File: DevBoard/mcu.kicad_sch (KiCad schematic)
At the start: 46 parts, among them J301 SWD, J302 UART debug, J303 Spare GPIO, SW301 RESET, U301 STM32WB1MMC

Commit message: Dev board: open-item pass, J104 diode, antenna keep-out, bring-up checklist
- D104 SS34 in series with the J104 bench input (reversed lead, back-feed).
- ANT_KEEPOUT rule area (no tracks/vias/pours, all copper layers) around
  the STM32WB1MMC antenna end, created by place_parts.py.
- D401 drawn unidirectional; header part numbers (PZ254V-11 family);
  shunt, J301 keying, B-constant, insulated-NTC, sheet-text and R201 notes.
- docs/devboard/bringup-config-checklist.md: every configuration item from
  both reviews in bring-up order, with review 2's precharge correction;
  review 1's 0 mV precharge line marked superseded.

Co-Authored-By: Claude Opus 5.5 <noreply@anthropic.com>
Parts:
- J301: Notes Keyed (pin 7 removed) so standard Cortex debug cables only 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 -> Keyed by its shroud (-K): Cortex 10-pin cables seat one way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
- J302: LCSC (none) -> C2937625; MPN (none) -> PZ254V-11-03P
- J303: LCSC (none) -> C492406; MPN (none) -> PZ254V-11-07P
- TH301: Notes TH1 port 1 stage -> TH1 port 1 stage. Murata NCP18XH103F03RB: B25/50 = 3380 K, 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
- TH302: Notes TH2 port 2 stage -> TH2 port 2 stage. Murata NCP18XH103F03RB: B25/50 = 3380 K, 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
- TH303: Notes TH3 connectors -> TH3 connectors. Murata NCP18XH103F03RB: B25/50 = 3380 K, B2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
- TH304: Notes TH4 heatsink pad -> TH4 heatsink pad. Murata NCP18XH103F03RB: B25/50 = 3380 K, 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
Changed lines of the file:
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@@
 			)
 		)
-		(property "Notes" "TH2 port 2 stage"
+		(property "Notes" "TH2 port 2 stage. Murata NCP18XH103F03RB: B25/50 = 3380 K, B25/85 = 3435 K (the \"B3435\" in the value); use Murata's R-T table in firmware"
 			(at 0 0 0)
 			(hide yes)
@@
 			)
 		)
-		(property "Notes" "TH3 connectors"
+		(property "Notes" "TH3 connectors. Murata NCP18XH103F03RB: B25/50 = 3380 K, B25/85 = 3435 K (the \"B3435\" in the value); use Murata's R-T table in firmware"
 			(at 0 0 0)
 			(hide yes)
@@
 			)
 		)
-		(property "Notes" "TH4 heatsink pad"
+		(property "Notes" "TH4 heatsink pad. Murata NCP18XH103F03RB: B25/50 = 3380 K, B25/85 = 3435 K (the \"B3435\" in the value); use Murata's R-T table in firmware"
 			(at 0 0 0)
 			(hide yes)
@@
 			)
 		)
-		(property "Notes" "Keyed (pin 7 removed) so standard Cortex debug cables only fit one way (review m15)"
+		(property "Notes" "Keyed by its shroud (-K): Cortex 10-pin cables seat one way only (review m15; all 10 pins fitted, pin 7 is NOT removed). Hand-fit, not in the JLC BOM"
 			(at -148.59 40.64 0)
 			(hide yes)
@@
 			)
 		)
-		(property "Notes" "TH1 port 1 stage"
+		(property "Notes" "TH1 port 1 stage. Murata NCP18XH103F03RB: B25/50 = 3380 K, B25/85 = 3435 K (the \"B3435\" in the value); use Murata's R-T table in firmware"
 			(at 0 0 0)
 			(hide yes)
@@
 			)
 		)
+		(property "LCSC" "C2937625"
+			(at 304.8 137.16 0)
+			(hide yes)
+			(show_name no)
+			(do_not_autoplace no)
+			(effects
+				(font
+					(size 1.27 1.27)
+				)
+			)
+		)
+		(property "MPN" "PZ254V-11-03P"
+			(at 304.8 137.16 0)
+			(hide yes)
+			(show_name no)
+			(do_not_autoplace no)
+			(effects
+				(font
+					(size 1.27 1.27)
+				)
+			)
+		)
 		(pin "1"
 		)
@@
 			(at 304.8 165.1 0)
 			(hide yes)
+			(show_name no)
+			(do_not_autoplace no)
+			(effects
+				(font
+					(size 1.27 1.27)
+				)
+			)
+		)
+		(property "LCSC" "C492406"
+			(at 304.8 165.1 0)
+			(hide yes)
+			(show_name no)
+			(do_not_autoplace no)
+			(effects
+				(font
+					(size 1.27 1.27)
+				)
+			)
+		)
+		(property "MPN" "PZ254V-11-07P"
+			(at 304.8 165.1 0)
+			(hide yes)

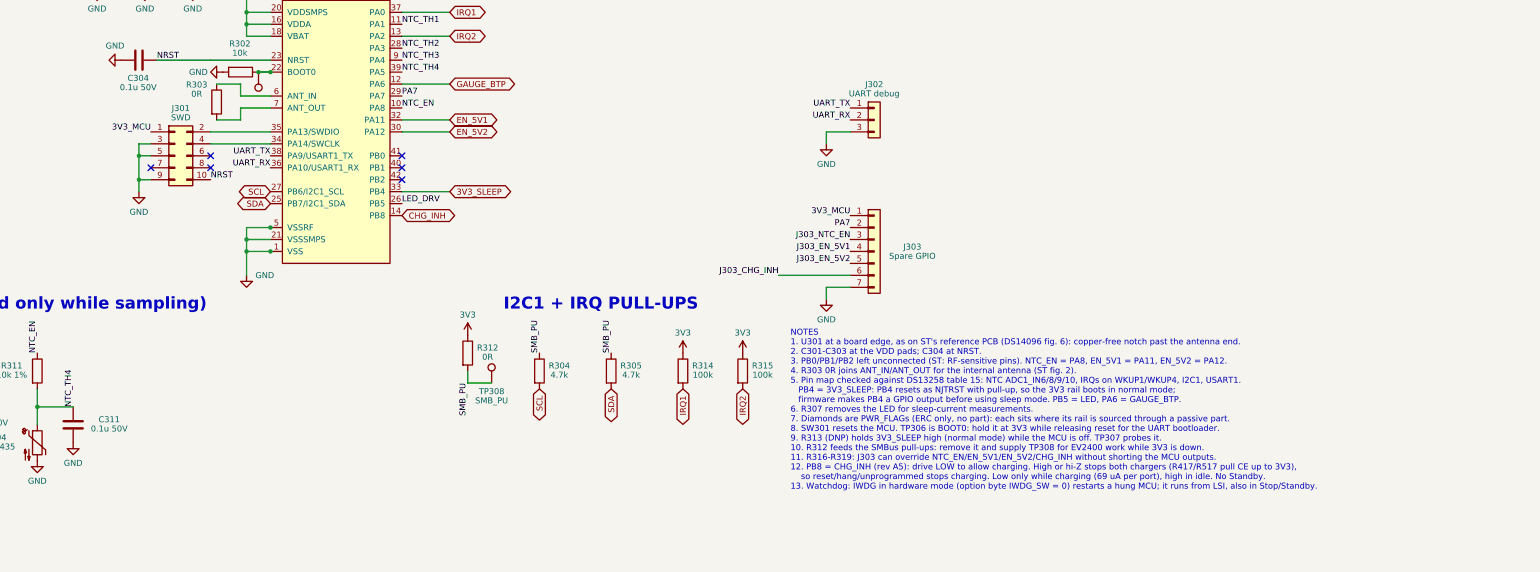
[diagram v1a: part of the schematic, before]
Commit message: Dev board: TH305 at the protection FETs; drop the gauge-BAT INA190 idea
- TH305 (10k NTC) between Q101/Q102 on PA7 / ADC1_IN2, same 10k 1 % /
  0.1 uF divider from NTC_EN (R320, C312). PA7 net renamed NTC_TH5, still
  on J303 pin 2. Placed beside C111; R320/C312 under J303.
- Optional third INA190 on the gauge BAT feed dropped: measure the gauge
  supply as the drop across R105 (100 R, 50-340 uA = 5-34 mV).

Co-Authored-By: Claude Opus 5.5 <noreply@anthropic.com>
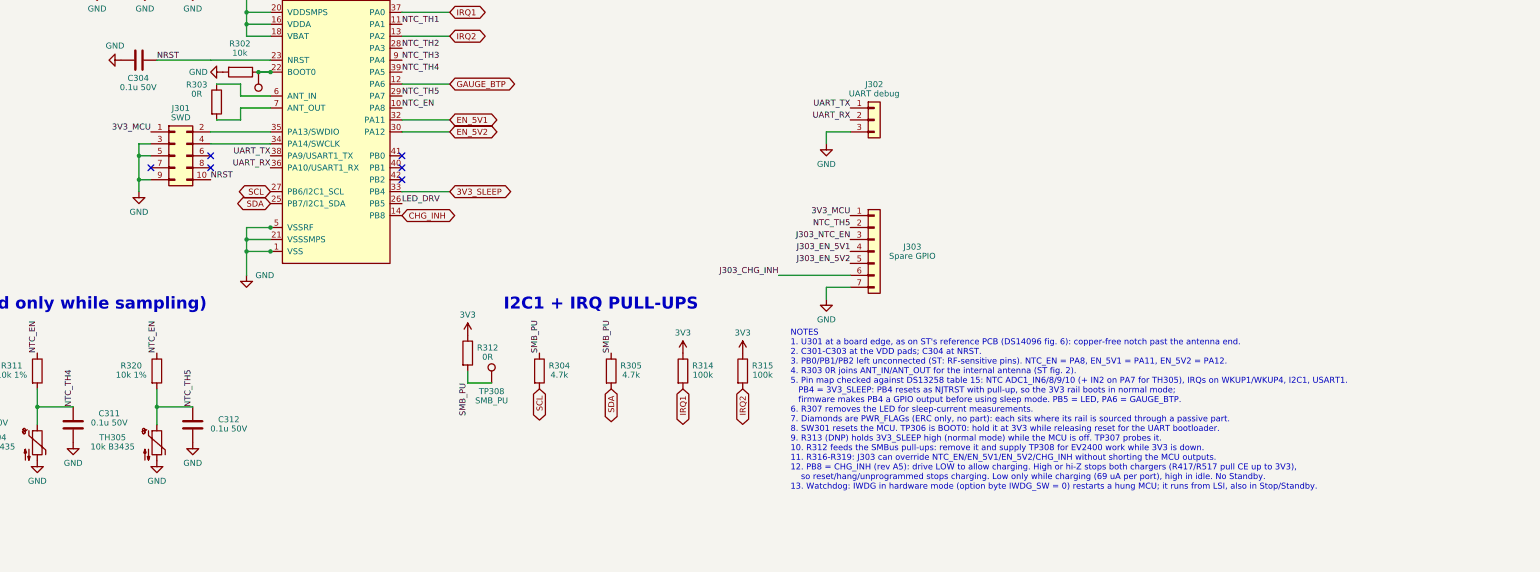
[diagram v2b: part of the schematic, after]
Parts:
- added C312: 0.1u 50V, Capacitor_SMD:C_0603_1608Metric, symbol Device:C
- added R320: 10k 1%, Resistor_SMD:R_0805_2012Metric, symbol Device:R
- added TH305: 10k B3435, Resistor_SMD:R_0603_1608Metric, symbol Device:Thermistor_NTC
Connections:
- net GND: now also C312.2, TH305.2
- net NTC_EN: now also R320.1
- net PA7 renamed NTC_TH5
- net NTC_TH5: now also C312.1, R320.2, TH305.1
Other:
- note added: "NOTES 1. U301 at a board edge, as on ST's reference PCB (DS14096 fig. 6): copper-free notch past the antenna end. 2. C301-C303 at the VDD pads; C304 at NRST. 3. PB0/PB1/PB2 left unconnected (ST: RF-sensitive pins). NTC_EN = PA8, EN_5V1 = PA11, EN_5V2 = PA12. 4. R303 0R joins ANT_IN/ANT_OUT for the internal antenna (ST fig. 2). 5. Pin map checked against DS13258 table 15: NTC ADC1_IN6/8/9/10 (+ IN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"
- note removed: "NOTES 1. U301 at a board edge, as on ST's reference PCB (DS14096 fig. 6): copper-free notch past the antenna end. 2. C301-C303 at the VDD pads; C304 at NRST. 3. PB0/PB1/PB2 left unconnected (ST: RF-sensitive pins). NTC_EN = PA8, EN_5V1 = PA11, EN_5V2 = PA12. 4. R303 0R joins ANT_IN/ANT_OUT for the internal antenna (ST fig. 2). 5. Pin map checked against DS13258 table 15: NTC ADC1_IN6/8/9/10, IRQs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"

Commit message: Dev board: holder tab hole, Samtec J301 land pattern, 3D models, measured USB-C STEP
- Cell holder footprint: add the dia 2.25 hole for the + terminal locating
  tab (from the rendered MYOUNG drawing; the holder could not seat flat).
- J301 on Samtec's recommended FTSH-1xx-DV land pattern with the -K shroud
  courtyard; J301 and the MCU title moved to fit.
- 3D models on 292 of 362 footprints: custom footprints borrow same-body
  KiCad models (pin 1 checked in renders); SMA and TS-1187A re-pointed to
  shipped models by place_parts.py.
- USB-C (J401/J501): STEP model measured from ShouHan's vector drawing
  (tools/drawing_extract, tools/make_3d_usbc.py) and verified by hidden-line
  overlays on all three views (3dmodels/verification).
- Placer: test-point labels sorted by reference; hidden only when no spot.
- docs/devboard/power-budget.md; renders in DevBoard/renders.

Co-Authored-By: Claude Opus 5.5 <noreply@anthropic.com>
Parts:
- J301: footprint Connector_PinHeader_1.27mm:PinHeader_2x05_P1.27mm_Vertical_SMD -> MonolithDev:Samtec_FTSH-105-01-xx-DV-K_2x05_P1.27mm
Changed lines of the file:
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@@
 			)
 		)
-		(property "Footprint" "Connector_PinHeader_1.27mm:PinHeader_2x05_P1.27mm_Vertical_SMD"
+		(property "Footprint" "MonolithDev:Samtec_FTSH-105-01-xx-DV-K_2x05_P1.27mm"
 			(at 156.21 144.78 0)
 			(hide yes)

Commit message: Dev board: cost-down pass (about $113 -> $80 per board at 5 boards)
Swaps from docs/devboard/cost-down-2026-10-14.md, datasheet-checked:
- L401/L501 XAL7030 -> SMMS1040-2R2M (Isat 18 A, Irms 12 A, 9 mOhm)
- L402/L502 SRP5030T -> APS0530M3R3H (new footprint L_Coilank_APS0530)
- L201 SRN4018TA -> FNR4030S100MT
- U203 TPS70950 -> HT7550-1, C204/C205 10 uF per Holtek's basic circuit
- C431/C434/C435 47 uF 1210 -> 22 uF 1206 (bank ~114 uF effective)
- JLC basic/preferred equivalents: D103, D401, R410/R412, C105/C206,
  C406, Q103 -> AO3400A
- D301 (out of stock) -> red KT-0603R
- R431/R531 -> bridged solder jumper
- 34 test loops -> bare pads; pin headers hand-soldered
- U301 bought from ST and consigned to JLC

ERC unchanged (0 errors, 8 expected GPIO-to-GND warnings).

Co-Authored-By: Claude Opus 5.5 <noreply@anthropic.com>
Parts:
- D301: value Green status -> Red status; LCSC C72043 -> C2286; MPN 19-217/GHC-YR1S2/3T -> KT-0603R (Hubei KENTO); Notes (none) -> Red 0603 (Vf 1.8-2.4 V), JLC basic: about 4 mA through R306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
- J302: LCSC C2937625 -> (none); Sourcing (none) -> Hand-solder, not JLC assembled (through-hole; LCSC C2937625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
- J303: LCSC C492406 -> (none); Sourcing (none) -> Hand-solder, not JLC assembled (through-hole; LCSC C492406 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
- R306: Notes InGaN green (Vf ~3 V): 330R gives ~1 mA from 3.3 V (1k gave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 -> 330R with the red KT-0603R (Vf ~2 V): about 4 mA from 3.3 V
- TP301, TP302, TP303, TP304, TP305, TP308: footprint MonolithDev:TestPoint_Harwin_S2761_0603 -> TestPoint:TestPoint_Pad_D1.5mm; LCSC C55121754 -> (none); MPN RH-S2761-46R (ronghe; Harwin S2761-46R equivalent) -> (none); now left out of the parts list
- U301: Notes LGA-77, JLC-placed only: check JLC stock at order time (LCS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 -> LGA-77: have JLC place it from consigned stock (JLC had 0 o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; Sourcing (none) -> Buy from ST eStore ($10.65 at 1, $9.87 at 10 on 2026-10-14)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
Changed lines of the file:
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@@
 			)
 		)
-		(property "Value" "Green status"
+		(property "Value" "Red status"
 			(at 71.43 239.77 0)
 			(show_name no)
@@
 			)
 		)
+		(property "Notes" "Red 0603 (Vf 1.8-2.4 V), JLC basic: about 4 mA through R306. The green Everlight 19-217 (C72043) went out of stock at JLC (cost-down 2026-10-14)"
+			(at 71.12 243.84 0)
+			(hide yes)
+			(show_name no)
+			(do_not_autoplace no)
+			(effects
+				(font
+					(size 1.27 1.27)
+				)
+			)
+		)
 		(property "Description" "Light emitting diode"
 			(at 71.12 243.84 0)
@@
 			)
 		)
-		(property "LCSC" "C72043"
+		(property "LCSC" "C2286"
 			(at 71.12 243.84 0)
 			(hide yes)
@@
 			)
 		)
-		(property "MPN" "19-217/GHC-YR1S2/3T"
+		(property "MPN" "KT-0603R (Hubei KENTO)"
 			(at 71.12 243.84 0)
 			(hide yes)
@@
 		(body_style 1)
 		(exclude_from_sim no)
-		(in_bom yes)
+		(in_bom no)
 		(on_board yes)
 		(in_pos_files yes)
@@
 			)
 		)
-		(property "Footprint" "MonolithDev:TestPoint_Harwin_S2761_0603"
+		(property "Footprint" "TestPoint:TestPoint_Pad_D1.5mm"
 			(at 223.52 193.04 0)
 			(hide yes)
@@
 			)
 		)
-		(property "LCSC" "C55121754"
-			(at 223.52 193.04 0)
-			(hide yes)
-			(show_name no)
-			(do_not_autoplace no)
-			(effects
-				(font
-					(size 1.27 1.27)
-				)
-			)
-		)
-		(property "MPN" "RH-S2761-46R (ronghe; Harwin S2761-46R equivalent)"
-			(at 223.52 193.04 0)
-			(hide yes)
-			(show_name no)
-			(do_not_autoplace no)
-			(effects
-				(font
-					(size 1.27 1.27)
-				)
-			)
-		)
 		(pin "1"
 		)
@@
 		(body_style 1)
 		(exclude_from_sim no)
-		(in_bom yes)
+		(in_bom no)
 		(on_board yes)
 		(in_pos_files yes)
@@
 			)
 		)
-		(property "Footprint" "MonolithDev:TestPoint_Harwin_S2761_0603"
+		(property "Footprint" "TestPoint:TestPoint_Pad_D1.5mm"
 			(at 236.22 264.16 0)
 			(hide yes)
@@
 			)
 		)
-		(property "LCSC" "C55121754"
-			(at 231.14 264.16 0)
-			(hide yes)
-			(show_name no)
-			(do_not_autoplace no)
-			(effects
-				(font
-					(size 1.27 1.27)
-				)
-			)
-		)
-		(property "MPN" "RH-S2761-46R (ronghe; Harwin S2761-46R equivalent)"
-			(at 231.14 264.16 0)
-			(hide yes)
-			(show_name no)
-			(do_not_autoplace no)
-			(effects
-				(font
-					(size 1.27 1.27)
-				)
-			)
-		)
 		(pin "1"
 		)
@@
 			)
 		)
+		(property "Sourcing" "Buy from ST eStore ($10.65 at 1, $9.87 at 10 on 2026-10-14) or DigiKey; consign to JLC for placement (LGA-77)"
+			(at 190.5 139.7 0)
+			(hide yes)
+			(show_name no)
+			(do_not_autoplace no)
+			(effects
+				(font
+					(size 1.27 1.27)
+				)
+			)
+		)
 		(property "Description" "STM32WB15 Bluetooth LE module with integrated antenna"
 			(at 190.5 139.7 0)
@@
 			)
 		)
-		(property "Notes" "LGA-77, JLC-placed only: check JLC stock at order time (LCSC had 0 on 2026-10-12); consign if needed"
+		(property "Notes" "LGA-77: have JLC place it from consigned stock (JLC had 0 on 2026-10-14). LCSC number kept only to identify the part"
 			(at 190.5 139.7 0)
 			(hide yes)
@@
 		(body_style 1)
 		(exclude_from_sim no)
-		(in_bom yes)
+		(in_bom no)
 		(on_board yes)
 		(in_pos_files yes)
@@
 			)
 		)
-		(property "Footprint" "MonolithDev:TestPoint_Harwin_S2761_0603"
+		(property "Footprint" "TestPoint:TestPoint_Pad_D1.5mm"
 			(at 276.86 264.16 0)
 			(hide yes)
@@
 			)
 		)
-		(property "LCSC" "C55121754"
-			(at 271.78 264.16 0)
-			(hide yes)
-			(show_name no)
-			(do_not_autoplace no)
-			(effects
-				(font
-					(size 1.27 1.27)
-				)
-			)
-		)
-		(property "MPN" "RH-S2761-46R (ronghe; Harwin S2761-46R equivalent)"
-			(at 271.78 264.16 0)
-			(hide yes)
-			(show_name no)
-			(do_not_autoplace no)
-			(effects
-				(font
-					(size 1.27 1.27)
-				)
-			)
-		)
 		(pin "1"
 		)
@@
 		(body_style 1)
 		(exclude_from_sim no)
-		(in_bom yes)
+		(in_bom no)
 		(on_board yes)
 		(in_pos_files yes)
@@
 			)
 		)
-		(property "Footprint" "MonolithDev:TestPoint_Harwin_S2761_0603"
+		(property "Footprint" "TestPoint:TestPoint_Pad_D1.5mm"
 			(at 215.9 264.16 0)
 			(hide yes)
@@
 			)
 		)
-		(property "LCSC" "C55121754"
-			(at 210.82 264.16 0)
-			(hide yes)
-			(show_name no)
-			(do_not_autoplace no)
-			(effects
-				(font
-					(size 1.27 1.27)
-				)
-			)
-		)
-		(property "MPN" "RH-S2761-46R (ronghe; Harwin S2761-46R equivalent)"
-			(at 210.82 264.16 0)
-			(hide yes)
-			(show_name no)
-			(do_not_autoplace no)
-			(effects
-				(font
-					(size 1.27 1.27)
-				)
-			)
-		)
 		(pin "1"
 		)
@@
 			)
 		)
-		(property "Notes" "InGaN green (Vf ~3 V): 330R gives ~1 mA from 3.3 V (1k gave ~0.5 mA, barely visible)"
+		(property "Notes" "330R with the red KT-0603R (Vf ~2 V): about 4 mA from 3.3 V"
 			(at 55.88 243.84 0)
 			(hide yes)
@@
 		(body_style 1)
 		(exclude_from_sim no)
-		(in_bom yes)
+		(in_bom no)
 		(on_board yes)
 		(in_pos_files yes)
@@
 			)
 		)
-		(property "Footprint" "MonolithDev:TestPoint_Harwin_S2761_0603"
+		(property "Footprint" "TestPoint:TestPoint_Pad_D1.5mm"
 			(at 256.54 264.16 0)
 			(hide yes)
@@
 			)
 		)
-		(property "LCSC" "C55121754"
-			(at 251.46 264.16 0)
-			(hide yes)
-			(show_name no)
-			(do_not_autoplace no)
-			(effects
-				(font
-					(size 1.27 1.27)
-				)
-			)
-		)
-		(property "MPN" "RH-S2761-46R (ronghe; Harwin S2761-46R equivalent)"
-			(at 251.46 264.16 0)
-			(hide yes)
-			(show_name no)
-			(do_not_autoplace no)
-			(effects
-				(font
-					(size 1.27 1.27)
-				)
-			)
-		)
 		(pin "1"
 		)
@@
 		(in_bom yes)
 		(on_board yes)
-		(in_pos_files yes)
+		(in_pos_files no)
 		(dnp no)
 		(property "Reference" "J302"
@@
 			)
 		)
-		(property "Description" "Generic connector, single row, 01x03, script generated (kicad-library-utils/schlib/autogen/connector/)"
+		(property "Sourcing" "Hand-solder, not JLC assembled (through-hole; LCSC C2937625 PZ254V-11-03P)"
 			(at 304.8 137.16 0)
 			(hide yes)
@@
 			)
 		)
-		(property "LCSC" "C2937625"
+		(property "Description" "Generic connector, single row, 01x03, script generated (kicad-library-utils/schlib/autogen/connector/)"
 			(at 304.8 137.16 0)
 			(hide yes)
@@
 		(in_bom yes)
 		(on_board yes)
-		(in_pos_files yes)
+		(in_pos_files no)
 		(dnp no)
 		(property "Reference" "J303"
@@
 			)
 		)
-		(property "Description" "Generic connector, single row, 01x07, script generated (kicad-library-utils/schlib/autogen/connector/)"
+		(property "Sourcing" "Hand-solder, not JLC assembled (through-hole; LCSC C492406 PZ254V-11-07P)"
 			(at 304.8 165.1 0)
 			(hide yes)
@@
 			)
 		)
-		(property "LCSC" "C492406"
+		(property "Description" "Generic connector, single row, 01x07, script generated (kicad-library-utils/schlib/autogen/connector/)"
 			(at 304.8 165.1 0)
 			(hide yes)
@@
 		(body_style 1)
 		(exclude_from_sim no)
-		(in_bom yes)
+		(in_bom no)
 		(on_board yes)
 		(in_pos_files yes)
@@
 			)
 		)
-		(property "Footprint" "MonolithDev:TestPoint_Harwin_S2761_0603"
+		(property "Footprint" "TestPoint:TestPoint_Pad_D1.5mm"
 			(at 297.18 264.16 0)
 			(hide yes)
@@
 			(at 292.1 264.16 0)
 			(hide yes)
-			(show_name no)
-			(do_not_autoplace no)
-			(effects
-				(font
-					(size 1.27 1.27)
-				)
-			)
-		)
-		(property "LCSC" "C55121754"
-			(at 292.1 264.16 0)
-			(hide yes)
-			(show_name no)
-			(do_not_autoplace no)
-			(effects
-				(font
-					(size 1.27 1.27)
-				)
-			)
-		)
-		(property "MPN" "RH-S2761-46R (ronghe; Harwin S2761-46R equivalent)"
-			(at 292.1 264.16 0)
-			(hide yes)

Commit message: Dev board schematic: tidy pass
- Title blocks on every sheet: rev A6, 2026-10-14, status line updated
  (was "Not reviewed, laid out, built or tested"); tidy_fields.py
  writes the same.
- Port sheet: the TPD4S201 block is titled with liquid detection
  ("CC/SBU PROTECTION (TPD4S201) + LIQUID DETECTION") and moved clear of
  the heading it collided with; I2Cc heading moved next to the EEPROM;
  PP5V heading clear of U405's GND.
- MCU sheet: test-point row out of the title block, with a heading;
  long NOTES lines wrapped inside the page border.
- Gauge sheet: cell-stack heading clear of its note; TP106 joins the
  test-point row.
- Top sheet: sheet index updated (BQ294700, TPD4S201, TH1-TH5) and
  spaced from the strap note and revision log; rev log line for the
  placement and this tidy.
- New tools/move_region.py moves a rectangle of a sheet (symbols,
  fields, wires, labels) by an offset.

Netlist identical before and after (265 nets); ERC 0 errors;
check_overlaps TOTAL 0.

Co-Authored-By: Claude Opus 5.5 <noreply@anthropic.com>
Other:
- note added: "TEST POINTS"
- moved on the sheet: TP301, TP302, TP303, TP304, TP305, TP309
